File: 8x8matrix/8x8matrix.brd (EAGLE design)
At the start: 63.5 x 60.5 mm, 7 parts

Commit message: tlc
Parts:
- removed JP2: (no value), SparkFun-Connectors:1X08
- removed R2: 1k, microbuilder:0805_NOTHERMALS
- removed U$2, U$3: CAT4016W, CAT4016:TSSOP24
- added IC1: 74595, SparkFun-DigitalIC:TSSOP16
- added U$14: TLC5947DAP, TLC5947:HTSSOP32DAP
- JP1: device SparkFun-Connectors:1X05 -> SparkFun-Connectors:1X06
- R1: value 1k -> (none); device microbuilder:0805_NOTHERMALS -> resistor:R0805
- moved JP1 58.9 mm to (3.56, 22.9)
- moved R1 17.0 mm to (27.4, 34.8), flipped to the top, turned to 0 degrees
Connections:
- removed net CLK: JP1.4, U$2.3, U$3.3
- removed net LATCH: JP1.5, U$2.4, U$3.4
- removed net N$35: JP2.8, U$1.P32
- removed net SOUT: U$2.2, U$3.22
- new net BLANK: JP1.3, U$14.2
- new net N$27: R1.2, U$14.31
- new net VCC: IC1.16
- new net XLAT: JP1.6, U$14.30
- net 5.0V: now also JP1.4, U$14.32; no longer JP1.2, U$2.24, U$3.24
- net GND: now also IC1.8, JP1.5, U$14.1, U$14.EXP; no longer JP1.1, R2.1, U$2.1, U$2.21, U$3.1, U$3.21
- net N$1: now also U$1.P1, U$14.5; no longer U$1.P8, U$2.5
- net N$10: now also U$1.P10, U$14.14; no longer U$1.P27, U$3.6
- net N$11: now also U$1.P11, U$14.15; no longer U$1.P26, U$3.7
- net N$12: now also U$1.P12, U$14.16; no longer U$1.P25, U$3.8
- net N$13: now also U$1.P13, U$14.17; no longer U$1.P24, U$3.9
- net N$14: now also U$1.P14, U$14.18; no longer U$1.P23, U$3.10
- net N$15: now also U$1.P15, U$14.19; no longer U$1.P22, U$3.11
- net N$16: now also U$1.P16, U$14.20; no longer U$1.P21, U$3.12
- net N$17: now also U$1.P21, U$14.21; no longer U$1.P16, U$3.13
- net N$18: now also U$1.P22, U$14.22; no longer U$1.P15, U$3.14
- net N$19: now also U$1.P23, U$14.23; no longer U$1.P14, U$3.15
- net N$2: now also U$1.P2, U$14.6; no longer U$1.P7, U$2.6
- net N$20: now also U$1.P24, U$14.24; no longer U$1.P13, U$3.16
- net N$21: now also U$1.P25, U$14.25; no longer U$1.P12, U$3.17
- net N$22: now also U$1.P26, U$14.26; no longer U$1.P11, U$3.18
- net N$23: now also U$1.P27, U$14.27; no longer U$1.P10, U$3.19
- net N$24: now also U$1.P28, U$14.28; no longer U$1.P9, U$3.20
- net N$25: now also IC1.1; no longer JP2.5
- net N$26: now also IC1.2, U$1.P30; no longer JP2.1, U$1.P20
- net N$28: now also JP1.2, U$14.3; no longer R1.2, U$3.23
- net N$29: now also IC1.3, U$1.P31; no longer R2.2, U$2.23
- net N$3: now also U$1.P3, U$14.7; no longer U$1.P6, U$2.7
- net N$30: now also IC1.4, U$1.P32; no longer JP2.2, U$1.P19
- net N$31: now also IC1.5, U$1.P20; no longer JP2.3, U$1.P18
- net N$32: now also IC1.6, U$1.P19; no longer JP2.4, U$1.P17
- net N$33: now also IC1.7, U$1.P18; no longer JP2.6, U$1.P30
- net N$34: now also IC1.9, U$1.P17; no longer JP2.7, U$1.P31
- net N$4: now also U$1.P4, U$14.8; no longer U$1.P5, U$2.8
- net N$5: now also U$1.P5, U$14.9; no longer U$1.P4, U$2.9
- net N$6: now also U$1.P6, U$14.10; no longer U$1.P3, U$2.10
- net N$7: now also U$1.P7, U$14.11; no longer U$1.P2, U$2.11
- net N$8: now also U$1.P8, U$14.12; no longer U$1.P1, U$2.12
- net N$9: now also U$1.P9, U$14.13; no longer U$1.P28, U$3.5
- net SIN: now also JP1.1, U$14.4; no longer JP1.3, U$3.2
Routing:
- net N$35: track 66.1 -> 0.00 mm
- net N$25: track 61.4 -> 13.0 mm
- net LATCH: track 44.9 -> 0.00 mm
- net CLK: track 43.3 -> 0.00 mm
- net XLAT: track 0.00 -> 29.5 mm
- net BLANK: track 0.00 -> 27.9 mm
- net 5.0V: track 53.7 -> 26.0 mm, vias 2 -> 0
- net N$30: track 30.2 -> 3.87 mm
- net N$28: track 2.32 -> 28.3 mm
- net N$26: track 33.8 -> 10.1 mm
- net N$33: track 62.8 -> 40.9 mm
- net SOUT: track 21.5 -> 0.00 mm
- net N$32: track 23.0 -> 38.0 mm
- net N$34: track 64.1 -> 49.7 mm
- net N$10: track 32.3 -> 19.1 mm
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- added copper zone on layer 1, net GND
- removed copper zone on layer 16, net GND
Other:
- board size 63.5 x 60.5 mm -> 60.4 x 60.5 mm

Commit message: tlc2
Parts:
- moved IC1 0.51 mm to (5.08, 53.1)
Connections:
- removed net VCC: IC1.16
- net 5.0V: now also IC1.16
- net N$34: now also IC1.15; no longer IC1.9
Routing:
- net N$34: track 49.7 -> 52.5 mm
- net N$32: track 38.0 -> 37.5 mm
- net N$26: track 10.1 -> 9.57 mm
- net N$25: track 13.0 -> 12.5 mm
- net N$30: track 3.87 -> 3.36 mm
- net N$29: track 7.17 -> 6.67 mm
- net N$33: track 40.9 -> 40.4 mm
- net N$31: track 35.1 -> 34.6 mm
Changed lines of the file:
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@@
 <element name="U$14" library="TLC5947" package="HTSSOP32DAP" value="TLC5947DAP" x="33.274" y="29.21"/>
 <element name="R1" library="resistor" package="R0805" value="" x="27.432" y="34.798"/>
-<element name="IC1" library="SparkFun-DigitalIC" package="TSSOP16" value="74595" x="4.572" y="53.086" rot="R90"/>
+<element name="IC1" library="SparkFun-DigitalIC" package="TSSOP16" value="74595" x="5.08" y="53.086" rot="R90"/>
 </elements>
 <signals>
@@
 <contactref element="JP1" pad="5"/>
 <contactref element="U$14" pad="EXP"/>
-<wire x1="26.582" y1="34.798" x2="33.274" y2="29.21" width="0" layer="19" extent="1-1"/>
+<contactref element="IC1" pad="8"/>
+<wire x1="33.274" y1="29.21" x2="26.582" y2="34.798" width="0" layer="19" extent="1-1"/>
 </signal>
 <signal name="5.0V">
@@
 <wire x1="26.924" y1="33.274" x2="28.285" y2="33.274" width="0.3048" layer="1"/>
 <wire x1="28.285" y1="33.274" x2="28.399" y2="33.16" width="0.3048" layer="1"/>
+<contactref element="IC1" pad="16"/>
+<wire x1="3.556" y1="30.504" x2="2.03" y2="50.861" width="0" layer="19" extent="1-1"/>
 </signal>
 <signal name="N$1">
@@
 <wire x1="5.612" y1="23.368" x2="3.556" y2="25.424" width="0.3048" layer="1"/>
 </signal>
-<signal name="VCC">
-<contactref element="IC1" pad="16"/>
-</signal>
 <signal name="N$25">
 <contactref element="IC1" pad="1"/>
 <contactref element="U$1" pad="P29"/>
-<wire x1="7.422" y1="50.861" x2="9.083" y2="50.861" width="0.3048" layer="1"/>
+<wire x1="7.93" y1="50.861" x2="9.083" y2="50.861" width="0.3048" layer="1"/>
 <wire x1="9.083" y1="50.861" x2="9.906" y2="50.038" width="0.3048" layer="1"/>
 <wire x1="9.906" y1="50.038" x2="15.748" y2="50.038" width="0.3048" layer="1"/>
@@
 <contactref element="IC1" pad="2"/>
 <contactref element="U$1" pad="P30"/>
-<wire x1="7.422" y1="51.511" x2="9.449" y2="51.511" width="0.3048" layer="1"/>
+<wire x1="7.93" y1="51.511" x2="9.449" y2="51.511" width="0.3048" layer="1"/>
 <wire x1="9.449" y1="51.511" x2="10.16" y2="50.8" width="0.3048" layer="1"/>
 <wire x1="10.16" y1="50.8" x2="13.97" y2="50.8" width="0.3048" layer="1"/>
@@
 <contactref element="IC1" pad="3"/>
 <contactref element="U$1" pad="P31"/>
-<wire x1="7.422" y1="52.161" x2="9.815" y2="52.161" width="0.3048" layer="1"/>
+<wire x1="7.93" y1="52.161" x2="9.815" y2="52.161" width="0.3048" layer="1"/>
 <wire x1="9.815" y1="52.161" x2="10.414" y2="51.562" width="0.3048" layer="1"/>
 <wire x1="10.414" y1="51.562" x2="12.192" y2="51.562" width="0.3048" layer="1"/>
@@
 <contactref element="IC1" pad="4"/>
 <contactref element="U$1" pad="P32"/>
-<wire x1="7.422" y1="52.811" x2="10.901" y2="52.811" width="0.3048" layer="1"/>
+<wire x1="7.93" y1="52.811" x2="10.901" y2="52.811" width="0.3048" layer="1"/>
 <wire x1="10.901" y1="52.811" x2="11.176" y2="53.086" width="0.3048" layer="1"/>
 </signal>
@@
 <contactref element="IC1" pad="5"/>
 <contactref element="U$1" pad="P20"/>
-<wire x1="7.422" y1="53.461" x2="9.519" y2="53.461" width="0.3048" layer="1"/>
+<wire x1="7.93" y1="53.461" x2="9.519" y2="53.461" width="0.3048" layer="1"/>
 <wire x1="9.519" y1="53.461" x2="10.414" y2="54.356" width="0.3048" layer="1"/>
 <wire x1="10.414" y1="54.356" x2="40.386" y2="54.356" width="0.3048" layer="1"/>
@@
 <contactref element="IC1" pad="6"/>
 <contactref element="U$1" pad="P19"/>
-<wire x1="7.422" y1="54.111" x2="9.153" y2="54.111" width="0.3048" layer="1"/>
+<wire x1="7.93" y1="54.111" x2="9.153" y2="54.111" width="0.3048" layer="1"/>
 <wire x1="9.153" y1="54.111" x2="10.16" y2="55.118" width="0.3048" layer="1"/>
 <wire x1="10.16" y1="55.118" x2="42.164" y2="55.118" width="0.3048" layer="1"/>
@@
 <contactref element="IC1" pad="7"/>
 <contactref element="U$1" pad="P18"/>
-<wire x1="7.422" y1="54.761" x2="8.787" y2="54.761" width="0.3048" layer="1"/>
+<wire x1="7.93" y1="54.761" x2="8.787" y2="54.761" width="0.3048" layer="1"/>
 <wire x1="8.787" y1="54.761" x2="9.906" y2="55.88" width="0.3048" layer="1"/>
 <wire x1="9.906" y1="55.88" x2="43.942" y2="55.88" width="0.3048" layer="1"/>
@@
 </signal>
 <signal name="N$34">
-<contactref element="IC1" pad="9"/>
+<contactref element="IC1" pad="15"/>
 <contactref element="U$1" pad="P17"/>
-<wire x1="49.276" y1="53.086" x2="45.72" y2="56.642" width="0.3048" layer="1"/>
-<wire x1="45.72" y1="56.642" x2="2.753" y2="56.642" width="0.3048" layer="1"/>
-<wire x1="2.753" y1="56.642" x2="1.522" y2="55.411" width="0.3048" layer="1"/>
+<wire x1="2.03" y1="51.511" x2="4.267" y2="51.511" width="0.3048" layer="1"/>
+<wire x1="4.267" y1="51.511" x2="5.334" y2="52.578" width="0.3048" layer="1"/>
+<wire x1="5.334" y1="52.578" x2="5.334" y2="55.372" width="0.3048" layer="1"/>
+<wire x1="5.334" y1="55.372" x2="6.604" y2="56.642" width="0.3048" layer="1"/>
+<wire x1="6.604" y1="56.642" x2="45.72" y2="56.642" width="0.3048" layer="1"/>
+<wire x1="45.72" y1="56.642" x2="49.276" y2="53.086" width="0.3048" layer="1"/>
 </signal>
 </signals>

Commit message: tlc3
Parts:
- removed IC1: 74595, SparkFun-DigitalIC:TSSOP16
- removed JP1: (no value), SparkFun-Connectors:1X06
- added JP2: M09, SparkFun-Connectors:1X09
- added R2: 0R, resistor:M1206
- added U$9: CD74HC238M, mylib:SO-16
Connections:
- removed net XLAT: JP1.6, U$14.30
- new net N$35: U$1.P29, U$9.7
- net 5.0V: now also JP2.6, U$9.16, U$9.6; no longer IC1.16, JP1.4
- net BLANK: now also JP2.3; no longer JP1.3
- net GND: now also JP2.5, R2.1, R2.2, U$9.4, U$9.5, U$9.8; no longer IC1.8, JP1.5
- net N$25: now also JP2.4, U$14.30; no longer IC1.1, U$1.P29
- net N$26: now also U$9.9; no longer IC1.2
- net N$28: now also JP2.2; no longer JP1.2
- net N$29: now also U$9.10; no longer IC1.3
- net N$30: now also U$9.11; no longer IC1.4
- net N$31: now also U$9.12; no longer IC1.5
- net N$32: now also U$9.13; no longer IC1.6
- net N$33: now also U$9.14; no longer IC1.7
- net N$34: now also U$9.15; no longer IC1.15
- net SIN: now also JP2.1; no longer JP1.1
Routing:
- net XLAT: track 29.5 -> 0.00 mm
- net 5.0V: track 26.0 -> 46.7 mm
- net N$25: track 12.5 -> 28.9 mm
- net N$35: track 0.00 -> 11.5 mm
- net N$33: track 40.4 -> 45.6 mm
- net N$26: track 9.57 -> 4.42 mm
- net N$32: track 37.5 -> 41.8 mm
- net N$31: track 34.6 -> 37.9 mm
- net N$29: track 6.67 -> 3.89 mm
- net N$34: track 52.5 -> 49.9 mm
- net BLANK: track 27.9 -> 26.7 mm
- net SIN: track 28.7 -> 29.7 mm
- net N$30: track 3.36 -> 4.00 mm
- net N$28: track 28.3 -> 27.8 mm

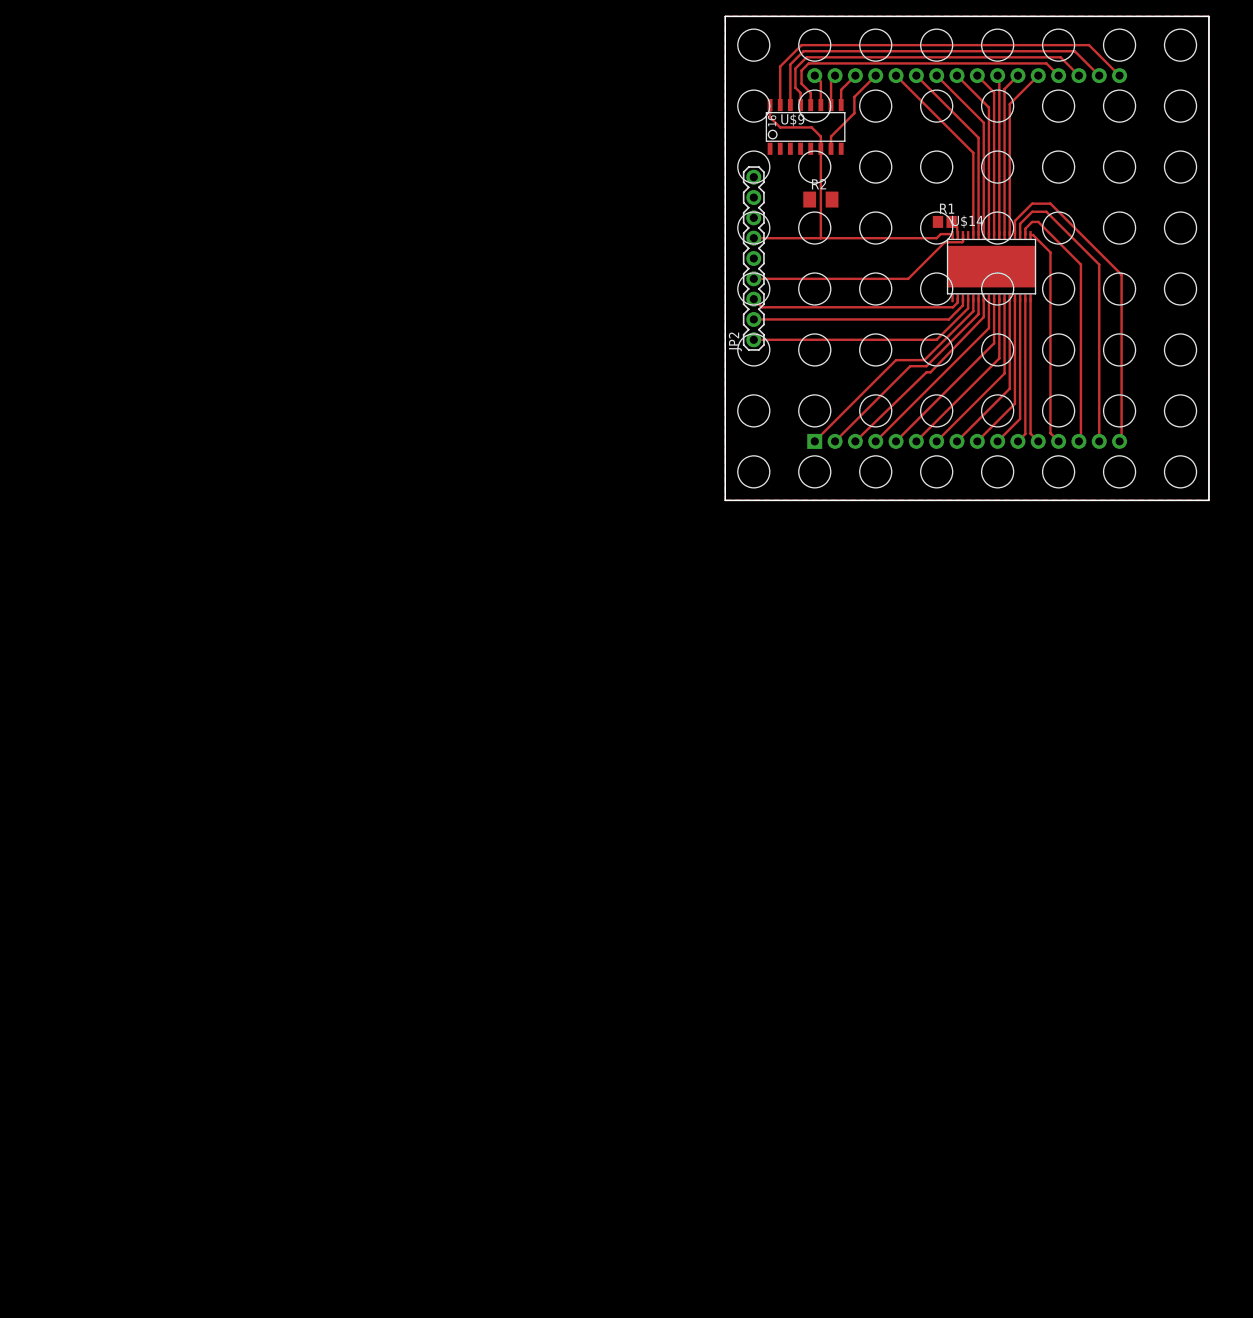
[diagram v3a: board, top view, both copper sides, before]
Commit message: tried adding FZTA92 darlingtons
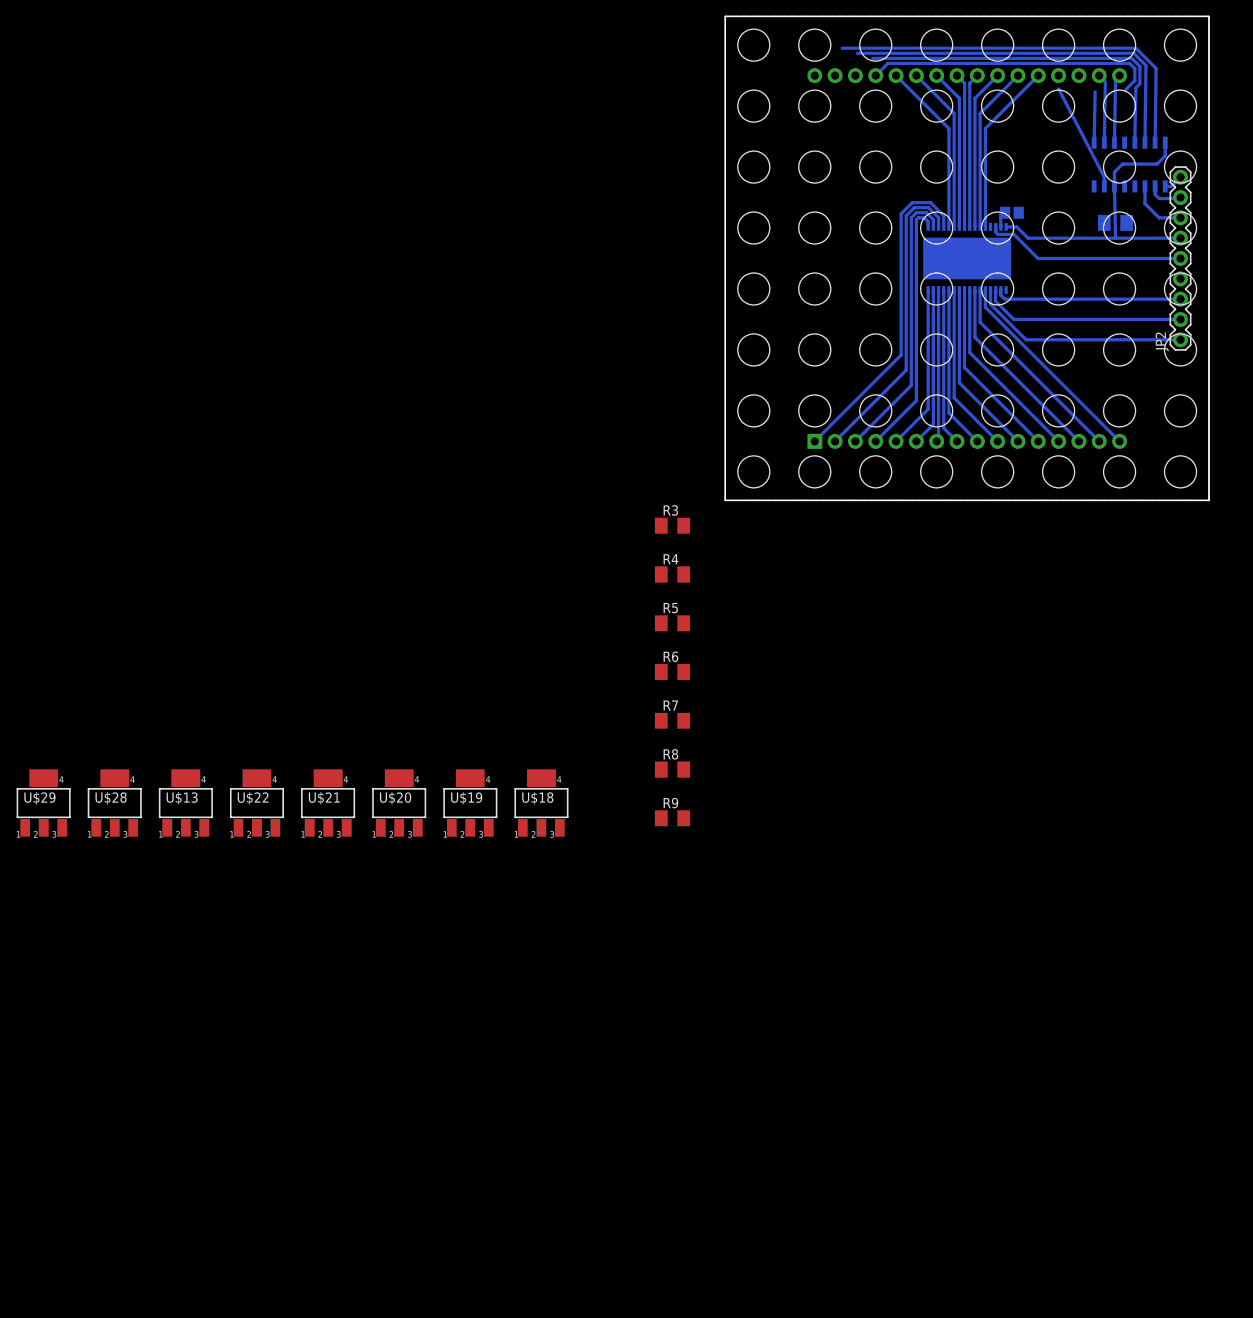
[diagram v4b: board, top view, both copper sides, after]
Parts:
- added R3, R4, R5, R6, R7, R8, R9: 0R, resistor:M1206
- added U$13, U$18, U$19, U$20, U$21, U$22, U$28, U$29: FZTA92, mylib:SOT223
- moved JP2 53.3 mm to (56.9, 20.1)
- moved U$9 40.8 mm to (50.5, 42.0), flipped to the bottom
- moved R2 36.9 mm to (48.8, 34.7), flipped to the bottom
- moved R1 8.46 mm to (35.8, 35.9), flipped to the bottom
- moved U$14 3.21 mm to (30.2, 30.2), flipped to the bottom
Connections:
- net N$28 renamed SCLK
- new net N$28: R5.2, U$18.1
- new net N$36: JP2.9, U$9.1
- new net N$37: JP2.8, U$9.2
- new net N$38: JP2.7, U$9.3
- new net N$39: R7.2, U$20.1
- new net N$40: R8.2, U$21.1
- new net N$41: R9.2, U$22.1
- new net N$42: U$1.P30, U$18.2, U$18.4
- new net N$43: U$1.P17, U$22.2, U$22.4
- new net N$44: U$1.P18, U$21.2, U$21.4
- new net N$45: R6.2, U$19.1
- new net N$46: U$1.P19, U$20.2, U$20.4
- new net N$47: U$1.P20, U$19.2, U$19.4
- new net N$48: R4.2, U$28.1
- new net N$49: R3.2, U$29.1
- new net N$50: U$1.P31, U$28.2, U$28.4
- new net N$51: U$1.P32, U$29.2, U$29.4
- new net XLAT: JP2.5, U$14.30
- net 5.0V: now also U$13.3, U$18.3, U$19.3, U$20.3, U$21.3, U$22.3, U$28.3, U$29.3
- net GND: now also JP2.4; no longer JP2.5
- net N$1: now also U$1.P16; no longer U$1.P1
- net N$10: now also U$1.P7; no longer U$1.P10
- net N$11: now also U$1.P6; no longer U$1.P11
- net N$12: now also U$1.P5; no longer U$1.P12
- net N$13: now also U$1.P4; no longer U$1.P13
- net N$14: now also U$1.P3; no longer U$1.P14
- net N$15: now also U$1.P2; no longer U$1.P15
- net N$16: now also U$1.P1; no longer U$1.P16
- net N$17: now also U$1.P28; no longer U$1.P21
- net N$18: now also U$1.P27; no longer U$1.P22
- net N$19: now also U$1.P26; no longer U$1.P23
- net N$2: now also U$1.P15; no longer U$1.P2
- net N$20: now also U$1.P25; no longer U$1.P24
- net N$21: now also U$1.P24; no longer U$1.P25
- net N$22: now also U$1.P23; no longer U$1.P26
- net N$23: now also U$1.P22; no longer U$1.P27
- net N$24: now also U$1.P21; no longer U$1.P28
- net N$25: now also U$13.1, U$9.12; no longer JP2.4, U$14.30
- net N$26: now also R6.1, U$9.7; no longer U$1.P30, U$9.9
- net N$29: now also R7.1, U$9.9; no longer U$1.P31, U$9.10
- net N$3: now also U$1.P14; no longer U$1.P3
- net N$30: now also R8.1, U$9.10; no longer U$1.P32, U$9.11
- net N$31: now also R9.1, U$9.11; no longer U$1.P20, U$9.12
- net N$32: now also U$1.P29, U$13.2, U$13.4; no longer U$1.P19, U$9.13
- net N$33: now also R5.1, U$9.13; no longer U$1.P18, U$9.14
- net N$34: now also R4.1, U$9.14; no longer U$1.P17, U$9.15
- net N$35: now also R3.1, U$9.15; no longer U$1.P29, U$9.7
- net N$4: now also U$1.P13; no longer U$1.P4
- net N$5: now also U$1.P12; no longer U$1.P5
- net N$6: now also U$1.P11; no longer U$1.P6
- net N$7: now also U$1.P10; no longer U$1.P7
- net N$8: now also U$1.P9; no longer U$1.P8
- net N$9: now also U$1.P8; no longer U$1.P9
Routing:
- net N$35: track 11.5 -> 49.6 mm
- net N$31: track 37.9 -> 7.88 mm
- net N$25: track 28.9 -> 0.00 mm
- net XLAT: track 0.00 -> 25.1 mm
- net N$26: track 4.42 -> 13.6 mm
- net N$38: track 0.00 -> 7.34 mm
- net 5.0V: track 46.7 -> 39.5 mm
- net N$32: track 41.8 -> 36.4 mm
- net N$13: track 27.4 -> 32.2 mm
- net N$37: track 0.00 -> 4.45 mm
- net N$30: track 4.00 -> 7.62 mm
- net N$34: track 49.9 -> 46.4 mm
- net BLANK: track 26.7 -> 23.3 mm
- net N$14: track 32.5 -> 35.1 mm
- net N$29: track 3.89 -> 6.35 mm
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- added copper zone on layer 16, net GND
- removed copper zone on layer 1, net GND
